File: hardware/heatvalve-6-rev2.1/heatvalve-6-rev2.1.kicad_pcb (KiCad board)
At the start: 4 copper layers, 120 x 75 mm, 105 parts, among them J1 USB4105-GF-A, J10 ONEWIRE 3, J11 I2C EXPANSION DNP, J2 MOTOR 1 4P4C, J3 MOTOR 2 4P4C, J4 MOTOR 3 4P4C, J5 MOTOR 4 4P4C, J6 MOTOR 5 4P4C, J7 MOTOR 6 4P4C, J8 ONEWIRE 1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

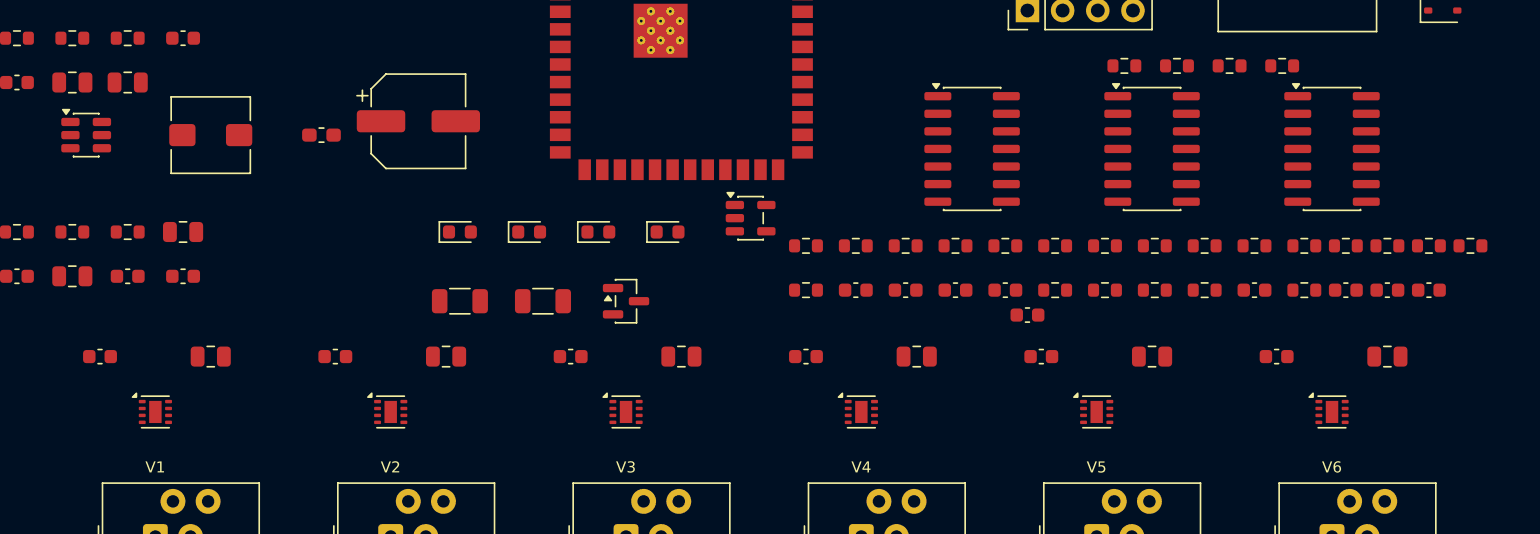
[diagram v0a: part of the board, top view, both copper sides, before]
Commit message: Add measurement and position model documentation for Rev 2.1
This commit introduces a new markdown file detailing the current, BEMF, engagement, and position model for the Rev 2.1 hardware. The document outlines the purpose of separating force measurement from motion measurement, describes mechanical landmarks, pin-engagement recognition, candidate tacho qualification, endstop and fault classification, flow mapping, and prototype gate considerations. It also includes references for further reading on sensorless position control and related topics.
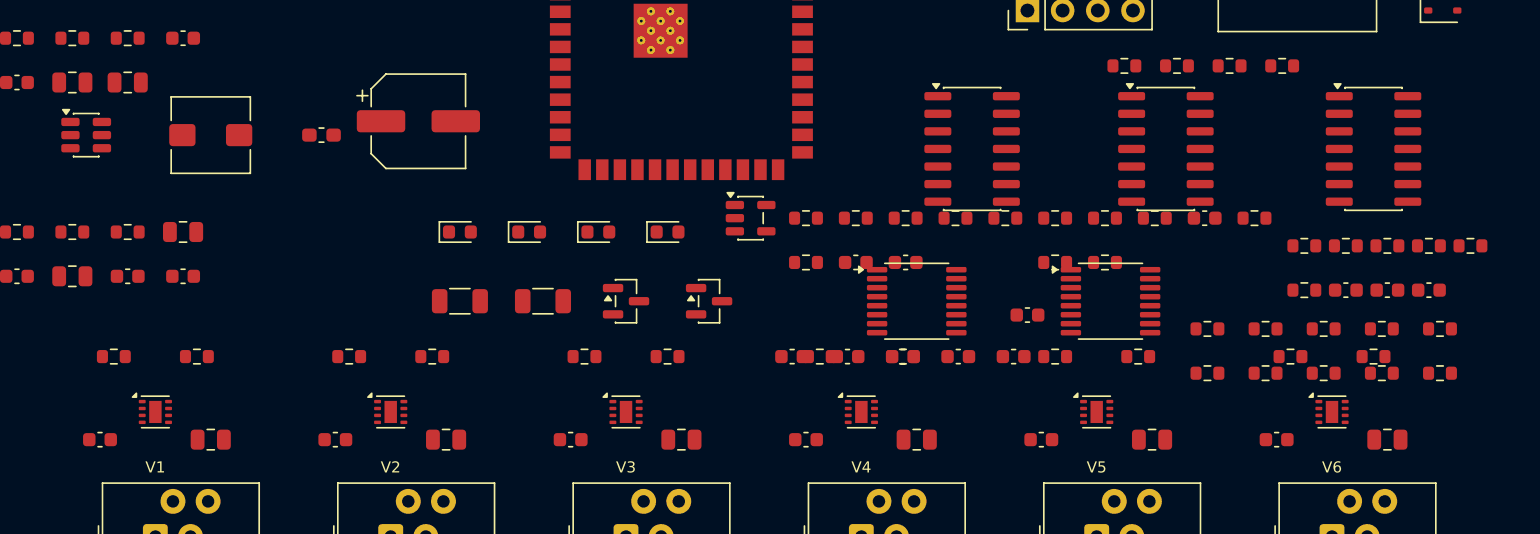
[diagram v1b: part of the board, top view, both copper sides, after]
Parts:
- removed C15: 100n, C_0603_1608Metric
- removed C16: 100n DNP, C_0603_1608Metric
- removed R17, R18: 100k, R_0603_1608Metric
- removed R19: 2.2k, R_0603_1608Metric
- removed R20, R22: 10k, R_0603_1608Metric
- removed R21: 1M, R_0603_1608Metric
- added C50: 100n, C_0603_1608Metric, F.Cu at (63.0, 44.0)
- added C51: 100n, C_0603_1608Metric, F.Cu at (67.0, 44.0)
- added C52: 4.7n, C_0603_1608Metric, F.Cu at (71.0, 44.0)
- added C53: 100n, C_0603_1608Metric, F.Cu at (75.0, 44.0)
- added C54: 100n DNP, C_0603_1608Metric, F.Cu at (79.0, 44.0)
- added D7: BAT54S BEMF ADC clamp, SOT-23, F.Cu at (57.0, 40.0)
- added R50: 90.9k 1%, R_0603_1608Metric, F.Cu at (93.0, 42.0)
- added R51: 47k 1%, R_0603_1608Metric, F.Cu at (97.2, 42.0)
- added R52: 90.9k 1%, R_0603_1608Metric, F.Cu at (101.4, 42.0)
- added R53: 47k 1%, R_0603_1608Metric, F.Cu at (105.6, 42.0)
- added R54: 1k, R_0603_1608Metric, F.Cu at (109.8, 42.0)
- added R55: 100k, R_0603_1608Metric, F.Cu at (93.0, 45.2)
- added R56: 10k, R_0603_1608Metric, F.Cu at (97.2, 45.2)
- added R57: 100k, R_0603_1608Metric, F.Cu at (101.4, 45.2)
- added R58: 1M, R_0603_1608Metric, F.Cu at (105.6, 45.2)
- added R59: 10k, R_0603_1608Metric, F.Cu at (109.8, 45.2)
- added R60: 100k, R_0603_1608Metric, F.Cu at (96.4, 34.0)
- added R61: 100k, R_0603_1608Metric, F.Cu at (82.0, 37.2)
- added R62: 100k, R_0603_1608Metric, F.Cu at (85.6, 37.2)
- added R70: 10k, R_0603_1608Metric, F.Cu at (14.0, 44.0)
- added R71: 10k, R_0603_1608Metric, F.Cu at (20.0, 44.0)
- added R72: 10k, R_0603_1608Metric, F.Cu at (31.0, 44.0)
- added R73: 10k, R_0603_1608Metric, F.Cu at (37.0, 44.0)
- added R74: 10k, R_0603_1608Metric, F.Cu at (48.0, 44.0)
- added R75: 10k, R_0603_1608Metric, F.Cu at (54.0, 44.0)
- added R76: 10k, R_0603_1608Metric, F.Cu at (65.0, 44.0)
- added R77: 10k, R_0603_1608Metric, F.Cu at (71.0, 44.0)
- added R78: 10k, R_0603_1608Metric, F.Cu at (82.0, 44.0)
- added R79: 10k, R_0603_1608Metric, F.Cu at (88.0, 44.0)
- added R80: 10k, R_0603_1608Metric, F.Cu at (99.0, 44.0)
- added R81: 10k, R_0603_1608Metric, F.Cu at (105.0, 44.0)
- added U13: 74HC4051, TSSOP-16_4.4x5mm_P0.65mm, F.Cu at (72.0, 40.0)
- added U14: 74HC4051, TSSOP-16_4.4x5mm_P0.65mm, F.Cu at (86.0, 40.0)
- R24: value 9.1k -> 18k
- RSH1: value 2.2R 1% -> 1.0R 1%
- moved C17 6.32 mm to (92.8, 34.0)
- moved R23 6.32 mm to (89.2, 34.0)
- moved C30 6.00 mm to (13.0, 50.0)
- moved C31 6.00 mm to (21.0, 50.0)
- moved C32 6.00 mm to (30.0, 50.0)
- moved C33 6.00 mm to (38.0, 50.0)
- moved C34 6.00 mm to (47.0, 50.0)
- moved C35 6.00 mm to (55.0, 50.0)
- moved C36 6.00 mm to (64.0, 50.0)
- moved C37 6.00 mm to (72.0, 50.0)
- moved C38 6.00 mm to (81.0, 50.0)
- moved C39 6.00 mm to (89.0, 50.0)
- moved C40 6.00 mm to (98.0, 50.0)
- moved C41 6.00 mm to (106.0, 50.0)
- moved U12 3.00 mm to (105.0, 29.0)
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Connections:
- U1 pad 12: unconnected-(U1-IO8-Pad12) -> /BEMF_SEL2
- U1 pad 5: unconnected-(U1-IO5-Pad5) -> /ADC_BEMF
- U1 pad 6: unconnected-(U1-IO6-Pad6) -> /BEMF_SEL0
- U1 pad 7: unconnected-(U1-IO7-Pad7) -> /BEMF_SEL1
- U10 pad 12: /VBIAS -> /BEMF_AC
- U10 pad 13: /OP_SPARE -> /BEMF_GAIN_FB
- U10 pad 14: /OP_SPARE -> /BEMF_TACH_AMP
- U10 pad 5: /TAC_IN -> /BEMF_DIFF_P
- U10 pad 6: /TAC_FB -> /BEMF_DIFF_N
- U10 pad 7: /TACHO_AMP -> /BEMF_RAW
- U11 pad 5: /TACHO_CMP -> /BEMF_TACH_AMP
